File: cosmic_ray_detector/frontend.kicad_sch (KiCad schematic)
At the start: 14 parts

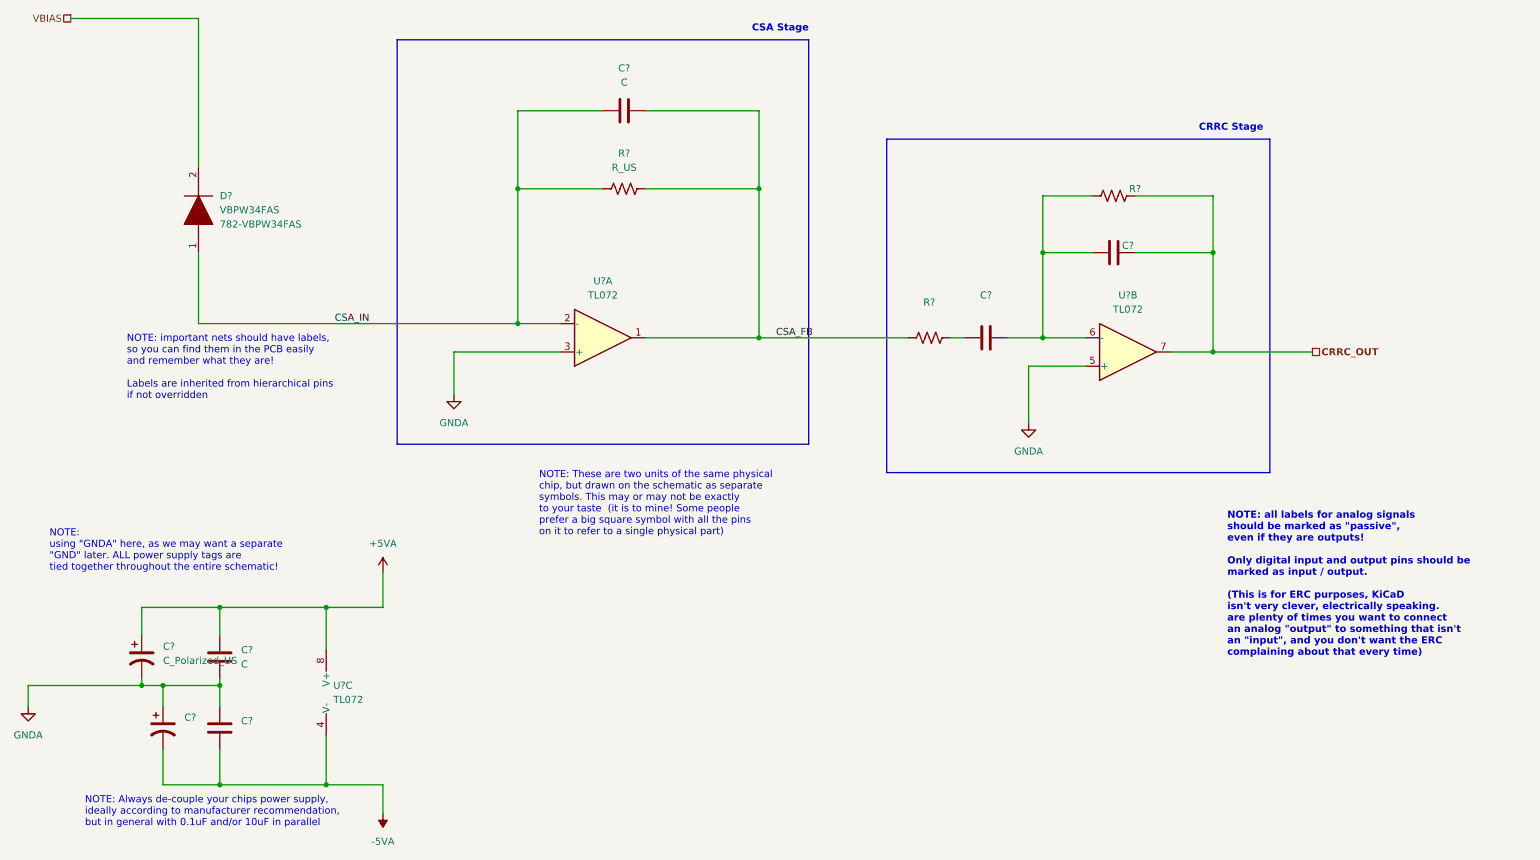
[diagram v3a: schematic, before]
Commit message: roughly finished schematic ready for annotation & ERC
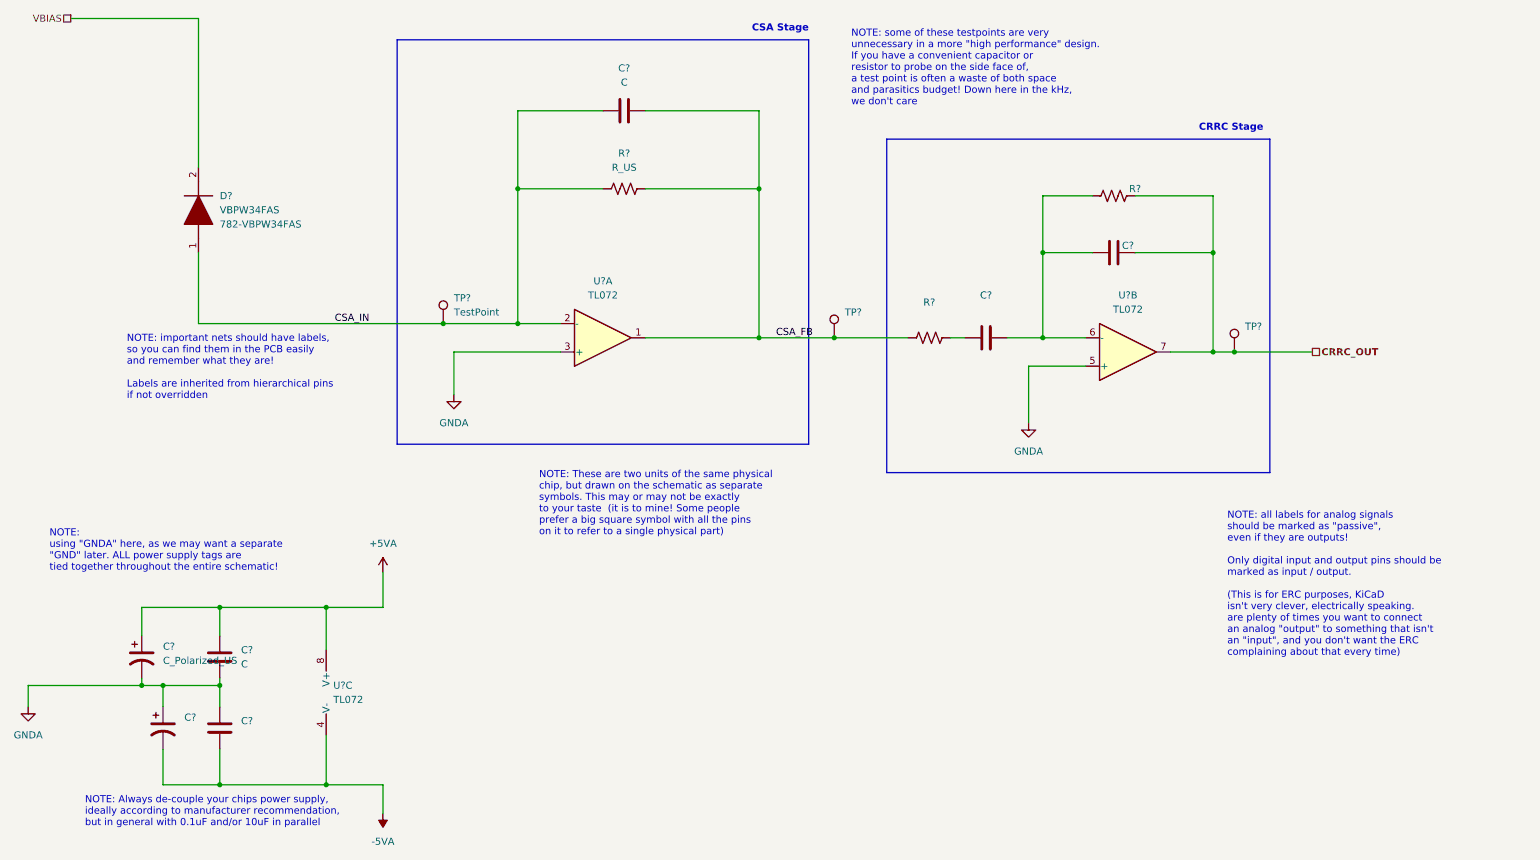
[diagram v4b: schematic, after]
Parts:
- added TP?: TestPoint, symbol Connector:TestPoint
- added TP? (x2): ~, symbol Connector:TestPoint
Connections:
- net CRRC_OUT: now also TP?.1
- net CSA_FB: now also TP?.1
- net CSA_IN: now also TP?.1
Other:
- note added: "NOTE: some of these testpoints are very unnecessary in a more "high performance" design. If you have a convenient capacitor or resistor to probe on the side face of, a test point is often a waste of both space and parasitics budget! Down here in the kHz, we don't care"
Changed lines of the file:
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@@
   (junction (at 204.47 105.41) (diameter 0) (color 0 0 0 0)
   )
+  (junction (at 167.132 105.41) (diameter 0) (color 0 0 0 0)
+  )
+  (junction (at 238.76 107.95) (diameter 0) (color 0 0 0 0)
+  )
   (junction (at 153.67 78.74) (diameter 0) (color 0 0 0 0)
   )
@@
   (junction (at 204.47 90.17) (diameter 0) (color 0 0 0 0)
   )
+  (junction (at 97.155 102.87) (diameter 0) (color 0 0 0 0)
+  )
+  (wire (pts (xy 238.76 107.95) (xy 252.73 107.95))
+    (stroke (width 0) (type default) (color 0 0 0 0))
+  )
   (wire (pts (xy 57.15 167.64) (xy 57.15 166.37))
     (stroke (width 0) (type default) (color 0 0 0 0))
@@
     (stroke (width 0) (type default) (color 0 0 0 0))
   )
+  (wire (pts (xy 167.132 105.41) (xy 180.34 105.41))
+    (stroke (width 0) (type default) (color 0 0 0 0))
+  )
   (wire (pts (xy 43.18 158.75) (xy 43.18 153.67))
     (stroke (width 0) (type default) (color 0 0 0 0))
@@
     (stroke (width 0) (type default) (color 0 0 0 0))
   )
-  (wire (pts (xy 153.67 105.41) (xy 180.34 105.41))
+  (wire (pts (xy 153.67 105.41) (xy 167.132 105.41))
     (stroke (width 0) (type default) (color 0 0 0 0))
   )
@@
     (stroke (width 0) (type default) (color 0 0 0 0))
   )
+  (wire (pts (xy 97.155 102.87) (xy 110.49 102.87))
+    (stroke (width 0) (type default) (color 0 0 0 0))
+  )
   (wire (pts (xy 204.47 105.41) (xy 204.47 90.17))
     (stroke (width 0) (type default) (color 0 0 0 0))
@@
     (stroke (width 0) (type default) (color 0 0 0 0))
   )
-  (wire (pts (xy 53.34 102.87) (xy 110.49 102.87))
+  (wire (pts (xy 53.34 102.87) (xy 97.155 102.87))
     (stroke (width 0) (type default) (color 0 0 0 0))
   )
@@
     (stroke (width 0) (type default) (color 0 0 0 0))
   )
-  (wire (pts (xy 234.95 107.95) (xy 252.73 107.95))
+  (wire (pts (xy 234.95 107.95) (xy 238.76 107.95))
     (stroke (width 0) (type default) (color 0 0 0 0))
   )
@@
   (wire (pts (xy 86.36 190.5) (xy 86.36 185.42))
     (stroke (width 0) (type default) (color 0 0 0 0))
+  )
+  (text "NOTE: some of these testpoints are very\nunnecessary in a more \"high performance\" design.\nIf you have a convenient capacitor or \nresistor to probe on the side face of,\na test point is often a waste of both space\nand parasitics budget! Down here in the kHz,\nwe don't care"
+    (at 170.18 64.008 0)
+    (effects (font (size 1.27 1.27)) (justify left bottom))
   )
   (text "CRRC Stage" (at 232.41 68.58 0)
@@
   (text "NOTE: all labels for analog signals\nshould be marked as \"passive\",\neven if they are outputs!\n\nOnly digital input and output pins should be\nmarked as input / output.\n\n(This is for ERC purposes, KiCaD \nisn't very clever, electrically speaking.\nare plenty of times you want to connect\nan analog \"output\" to something that isn't\nan \"input\", and you don't want the ERC\ncomplaining about that every time)"
     (at 237.49 162.56 0)
-    (effects (font (size 1.27 1.27) bold) (justify left bottom))
+    (effects (font (size 1.27 1.27)) (justify left bottom))
   )
   (text "NOTE: important nets should have labels,\nso you can find them in the PCB easily\nand remember what they are!\n\nLabels are inherited from hierarchical pins\nif not overridden"
@@
     (pin "1")
   )
+  (symbol (lib_id "Connector:TestPoint") (at 97.155 102.87 0) (unit 1)
+    (in_bom yes) (on_board yes) (fields_autoplaced)
+    (property "Reference" "TP?" (id 0) (at 99.06 98.2979 0)
+      (effects (font (size 1.27 1.27)) (justify left))
+    )
+    (property "Value" "TestPoint" (id 1) (at 99.06 100.8379 0)
+      (effects (font (size 1.27 1.27)) (justify left))
+    )
+    (property "Footprint" "" (id 2) (at 102.235 102.87 0)
+      (effects (font (size 1.27 1.27)) hide)
+    )
+    (property "Datasheet" "~" (id 3) (at 102.235 102.87 0)
+      (effects (font (size 1.27 1.27)) hide)
+    )
+    (pin "1")
+  )
   (symbol (lib_id "power:GNDA") (at 22.86 171.45 0) (unit 1)
     (in_bom yes) (on_board yes) (fields_autoplaced)
@@
     (pin "1")
     (pin "2")
+  )
+  (symbol (lib_id "Connector:TestPoint") (at 167.132 105.41 0) (unit 1)
+    (in_bom yes) (on_board yes) (fields_autoplaced)
+    (property "Reference" "TP?" (id 0) (at 169.037 100.8379 0)
+      (effects (font (size 1.27 1.27)) (justify left))
+    )
+    (property "Value" "~" (id 1) (at 169.037 103.3779 0)
+      (effects (font (size 1.27 1.27)) (justify left))
+    )
+    (property "Footprint" "" (id 2) (at 172.212 105.41 0)
+      (effects (font (size 1.27 1.27)) hide)
+    )
+    (property "Datasheet" "~" (id 3) (at 172.212 105.41 0)
+      (effects (font (size 1.27 1.27)) hide)
+    )
+    (pin "1")
   )
   (symbol (lib_id "Amplifier_Operational:TL072") (at 125.73 105.41 0) (mirror x) (unit 1)
@@
     (pin "8")
   )
+  (symbol (lib_id "Connector:TestPoint") (at 238.76 107.95 0) (unit 1)
+    (in_bom yes) (on_board yes) (fields_autoplaced)
+    (property "Reference" "TP?" (id 0) (at 240.665 103.3779 0)
+      (effects (font (size 1.27 1.27)) (justify left))
+    )
+    (property "Value" "~" (id 1) (at 240.665 105.9179 0)
+      (effects (font (size 1.27 1.27)) (justify left))
+    )
+    (property "Footprint" "" (id 2) (at 243.84 107.95 0)
+      (effects (font (size 1.27 1.27)) hide)
+    )
+    (property "Datasheet" "~" (id 3) (at 243.84 107.95 0)
+      (effects (font (size 1.27 1.27)) hide)
+    )
+    (pin "1")
+  )
 )

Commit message: annotated schematic
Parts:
- gave numbers to parts that had none: 15
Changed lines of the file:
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@@
   (symbol (lib_id "power:-5VA") (at 86.36 190.5 180) (unit 1)
     (in_bom yes) (on_board yes) (fields_autoplaced)
-    (property "Reference" "#PWR?" (id 0) (at 86.36 193.04 0)
+    (property "Reference" "#PWR09" (id 0) (at 86.36 193.04 0)
       (effects (font (size 1.27 1.27)) hide)
     )
@@
   (symbol (lib_id "Amplifier_Operational:TL072") (at 219.71 107.95 0) (mirror x) (unit 2)
     (in_bom yes) (on_board yes) (fields_autoplaced)
-    (property "Reference" "U?" (id 0) (at 219.71 97.79 0))
+    (property "Reference" "U1" (id 0) (at 219.71 97.79 0))
     (property "Value" "TL072" (id 1) (at 219.71 100.33 0))
     (property "Footprint" "" (id 2) (at 219.71 107.95 0)
@@
   (symbol (lib_id "Device:R_US") (at 217.17 80.01 90) (unit 1)
     (in_bom yes) (on_board yes)
-    (property "Reference" "R?" (id 0) (at 220.98 78.74 90))
+    (property "Reference" "R4" (id 0) (at 220.98 78.74 90))
     (property "Value" "~" (id 1) (at 217.17 76.2 90))
     (property "Footprint" "" (id 2) (at 217.424 78.994 90)
@@
   (symbol (lib_id "Device:C") (at 194.31 105.41 90) (unit 1)
     (in_bom yes) (on_board yes) (fields_autoplaced)
-    (property "Reference" "C?" (id 0) (at 194.31 97.79 90))
+    (property "Reference" "C7" (id 0) (at 194.31 97.79 90))
     (property "Value" "~" (id 1) (at 194.31 100.33 90))
     (property "Footprint" "" (id 2) (at 198.12 104.4448 0)
@@
   (symbol (lib_id "Device:R_US") (at 129.54 78.74 90) (unit 1)
     (in_bom yes) (on_board yes) (fields_autoplaced)
-    (property "Reference" "R?" (id 0) (at 129.54 72.39 90))
+    (property "Reference" "R2" (id 0) (at 129.54 72.39 90))
     (property "Value" "R_US" (id 1) (at 129.54 74.93 90))
     (property "Footprint" "" (id 2) (at 129.794 77.724 90)
@@
   (symbol (lib_id "power:GNDA") (at 201.93 120.65 0) (unit 1)
     (in_bom yes) (on_board yes) (fields_autoplaced)
-    (property "Reference" "#PWR?" (id 0) (at 201.93 127 0)
+    (property "Reference" "#PWR011" (id 0) (at 201.93 127 0)
       (effects (font (size 1.27 1.27)) hide)
     )
@@
   (symbol (lib_id "cosmic_ray_symbols:VBPW34FAS") (at 53.34 74.93 270) (unit 1)
     (in_bom yes) (on_board yes) (fields_autoplaced)
-    (property "Reference" "D?" (id 0) (at 57.15 80.0099 90)
+    (property "Reference" "D1" (id 0) (at 57.15 80.0099 90)
       (effects (font (size 1.27 1.27)) (justify left))
     )
@@
   (symbol (lib_id "Device:C") (at 57.15 162.56 0) (unit 1)
     (in_bom yes) (on_board yes) (fields_autoplaced)
-    (property "Reference" "C?" (id 0) (at 60.96 161.2899 0)
+    (property "Reference" "C4" (id 0) (at 60.96 161.2899 0)
       (effects (font (size 1.27 1.27)) (justify left))
     )
@@
   (symbol (lib_id "power:+5VA") (at 86.36 147.32 0) (unit 1)
     (in_bom yes) (on_board yes) (fields_autoplaced)
-    (property "Reference" "#PWR?" (id 0) (at 86.36 151.13 0)
+    (property "Reference" "#PWR08" (id 0) (at 86.36 151.13 0)
       (effects (font (size 1.27 1.27)) hide)
     )
@@
   (symbol (lib_id "Device:C_Polarized_US") (at 46.99 175.26 0) (unit 1)
     (in_bom yes) (on_board yes) (fields_autoplaced)
-    (property "Reference" "C?" (id 0) (at 50.8 173.3549 0)
+    (property "Reference" "C3" (id 0) (at 50.8 173.3549 0)
       (effects (font (size 1.27 1.27)) (justify left))
     )
@@
   (symbol (lib_id "Device:R_US") (at 184.15 105.41 90) (unit 1)
     (in_bom yes) (on_board yes) (fields_autoplaced)
-    (property "Reference" "R?" (id 0) (at 184.15 99.06 90))
+    (property "Reference" "R3" (id 0) (at 184.15 99.06 90))
     (property "Value" "~" (id 1) (at 184.15 101.6 90))
     (property "Footprint" "" (id 2) (at 184.404 104.394 90)
@@
   (symbol (lib_id "Device:C") (at 217.17 90.17 90) (unit 1)
     (in_bom yes) (on_board yes)
-    (property "Reference" "C?" (id 0) (at 219.71 88.9 90))
+    (property "Reference" "C8" (id 0) (at 219.71 88.9 90))
     (property "Value" "~" (id 1) (at 217.17 85.09 90))
     (property "Footprint" "" (id 2) (at 220.98 89.2048 0)
@@
   (symbol (lib_id "Device:C_Polarized_US") (at 43.18 162.56 0) (unit 1)
     (in_bom yes) (on_board yes) (fields_autoplaced)
-    (property "Reference" "C?" (id 0) (at 46.99 160.6549 0)
+    (property "Reference" "C2" (id 0) (at 46.99 160.6549 0)
       (effects (font (size 1.27 1.27)) (justify left))
     )
@@
   (symbol (lib_id "Device:C") (at 129.54 64.77 90) (unit 1)
     (in_bom yes) (on_board yes) (fields_autoplaced)
-    (property "Reference" "C?" (id 0) (at 129.54 57.15 90))
+    (property "Reference" "C6" (id 0) (at 129.54 57.15 90))
     (property "Value" "C" (id 1) (at 129.54 59.69 90))
     (property "Footprint" "" (id 2) (at 133.35 63.8048 0)
@@
   (symbol (lib_id "power:GNDA") (at 99.06 115.57 0) (unit 1)
     (in_bom yes) (on_board yes) (fields_autoplaced)
-    (property "Reference" "#PWR?" (id 0) (at 99.06 121.92 0)
+    (property "Reference" "#PWR010" (id 0) (at 99.06 121.92 0)
       (effects (font (size 1.27 1.27)) hide)
     )
@@
   (symbol (lib_id "Connector:TestPoint") (at 97.155 102.87 0) (unit 1)
     (in_bom yes) (on_board yes) (fields_autoplaced)
-    (property "Reference" "TP?" (id 0) (at 99.06 98.2979 0)
+    (property "Reference" "TP1" (id 0) (at 99.06 98.2979 0)
       (effects (font (size 1.27 1.27)) (justify left))
     )
@@
   (symbol (lib_id "power:GNDA") (at 22.86 171.45 0) (unit 1)
     (in_bom yes) (on_board yes) (fields_autoplaced)
-    (property "Reference" "#PWR?" (id 0) (at 22.86 177.8 0)
+    (property "Reference" "#PWR07" (id 0) (at 22.86 177.8 0)
       (effects (font (size 1.27 1.27)) hide)
     )
@@
   (symbol (lib_id "Device:C") (at 57.15 175.26 0) (unit 1)
     (in_bom yes) (on_board yes) (fields_autoplaced)
-    (property "Reference" "C?" (id 0) (at 60.96 173.9899 0)
+    (property "Reference" "C5" (id 0) (at 60.96 173.9899 0)
       (effects (font (size 1.27 1.27)) (justify left))
     )
@@
   (symbol (lib_id "Connector:TestPoint") (at 167.132 105.41 0) (unit 1)
     (in_bom yes) (on_board yes) (fields_autoplaced)
-    (property "Reference" "TP?" (id 0) (at 169.037 100.8379 0)
+    (property "Reference" "TP2" (id 0) (at 169.037 100.8379 0)
       (effects (font (size 1.27 1.27)) (justify left))
     )
@@
   (symbol (lib_id "Amplifier_Operational:TL072") (at 125.73 105.41 0) (mirror x) (unit 1)
     (in_bom yes) (on_board yes) (fields_autoplaced)
-    (property "Reference" "U?" (id 0) (at 125.73 95.25 0))
+    (property "Reference" "U1" (id 0) (at 125.73 95.25 0))
     (property "Value" "TL072" (id 1) (at 125.73 97.79 0))
     (property "Footprint" "" (id 2) (at 125.73 105.41 0)
@@
   (symbol (lib_id "Amplifier_Operational:TL072") (at 78.74 168.91 0) (unit 3)
     (in_bom yes) (on_board yes) (fields_autoplaced)
-    (property "Reference" "U?" (id 0) (at 77.47 167.6399 0)
+    (property "Reference" "U1" (id 0) (at 77.47 167.6399 0)
       (effects (font (size 1.27 1.27)) (justify left))
     )
@@
   (symbol (lib_id "Connector:TestPoint") (at 238.76 107.95 0) (unit 1)
     (in_bom yes) (on_board yes) (fields_autoplaced)
-    (property "Reference" "TP?" (id 0) (at 240.665 103.3779 0)
-      (effects (font (size 1.27 1.27)) (justify left))
-    )
+    (property "Reference" "TP3" (id 0) (at 240.665 103.3779 0)
+      (effects (font (size 1.27 1.27)) (justify left))
+    )

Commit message: add more 3d parts symbols to library
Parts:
- D1: footprint VBPW34FAS -> (none)
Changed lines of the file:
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@@
       (effects (font (size 1.27 1.27)) (justify left))
     )
-    (property "Footprint" "VBPW34FAS" (id 2) (at 53.34 86.36 0)
+    (property "Footprint" "" (id 2) (at 53.34 86.36 0)
       (effects (font (size 1.27 1.27)) (justify left) hide)
     )
